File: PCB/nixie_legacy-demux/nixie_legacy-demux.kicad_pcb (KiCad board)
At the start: 2 copper layers, 106.7 x 112 mm, 37 parts, among them J3 HEADER_18, J5 HEADER_4, K155ID1 K155ID1

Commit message: Adding demux PCB v1: uses resistor network for 100k, has npn on board but pnp is on digit board
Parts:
- removed the 22pF at (123.2, 103.9)
- removed the 22pF at (124.5, 122.4)
- removed R 100k: 100k, Resistor_THT:R_Axial_DIN0207_L6.3mm_D2.5mm_P7.62mm_Horizontal (x5)
- removed the R 470k at (70.6, 15.0)
- added 100k Network: 100k, Resistor_THT:R_Array_SIP7, F.Cu at (126.0, 68.1)
- added 22pF: 22pF, Capacitor_THT:C_Disc_D3.0mm_W1.6mm_P2.50mm, F.Cu at (125.0, 106.2)
- added 22pF: 22pF, Capacitor_THT:C_Disc_D3.0mm_W1.6mm_P2.50mm, F.Cu at (125.0, 121.4)
- R 3k3: renamed from R 3.3k (x2)
- R 470k: renamed from R6
- moved R 470k 59.2 mm to (119.4, 77.5)
- moved R 470k 55.7 mm to (114.8, 71.4), turned to 180 degrees
- moved R 470k 55.3 mm to (114.8, 77.5), turned to 180 degrees
- moved R 470k 55.2 mm to (114.8, 74.4), turned to 180 degrees
- moved MPSA42 53.5 mm to (121.9, 86.6)
- moved R 33k 50.0 mm to (114.8, 90.7), turned to 180 degrees
- moved MPSA42 49.0 mm to (114.6, 86.6)
- moved R 470k 48.7 mm to (119.4, 74.4)
- moved R 33k 48.5 mm to (114.8, 96.8), turned to 180 degrees
- moved R 33k 47.9 mm to (114.8, 93.7), turned to 180 degrees
- moved MPSA42 47.6 mm to (107.2, 86.6)
- moved MPSA42 38.7 mm to (127.0, 81.0), turned to 180 degrees
- moved R 470k 38.6 mm to (119.4, 71.4)
- moved GND,Sel,Up,Dn 30.4 mm to (119.4, 151.4), turned to 90 degrees
- moved J3 27.5 mm to (134.6, 88.1), turned to 180 degrees
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- renumbered ATMEGA328P to ATmega328p, J5 to GND,Sel,Up,Dn
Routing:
- net 5v: track 0.00 -> 161.5 mm
- net 200v: track 0.00 -> 104.7 mm
- net 5: track 0.00 -> 44.8 mm
- net 1: track 0.00 -> 40.7 mm
- net 9: track 0.00 -> 38.6 mm
- net digit6lsb: track 0.00 -> 37.8 mm
- net Net-(J5-Pad4): track 0.00 -> 37.6 mm
- net Net-(R18-Pad2): track 0.00 -> 35.5 mm
- net 8: track 0.00 -> 34.7 mm
- net Net-(J2-Pad7): track 0.00 -> 34.4 mm
- net 0: track 0.00 -> 34.3 mm
- net 4: track 0.00 -> 34.3 mm
- net Net-(U1-Pad13): track 0.00 -> 34.1 mm
- net Net-(J5-Pad3): track 0.00 -> 33.2 mm
- net Net-(U1-Pad14): track 0.00 -> 33.1 mm
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- added copper zone on B.Cu, net GND
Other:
- board size 106.7 x 112 mm -> 35.6 x 99.1 mm
- board text added: "Nixie Demux v1"
- board text added: "WARNING: High Voltage"

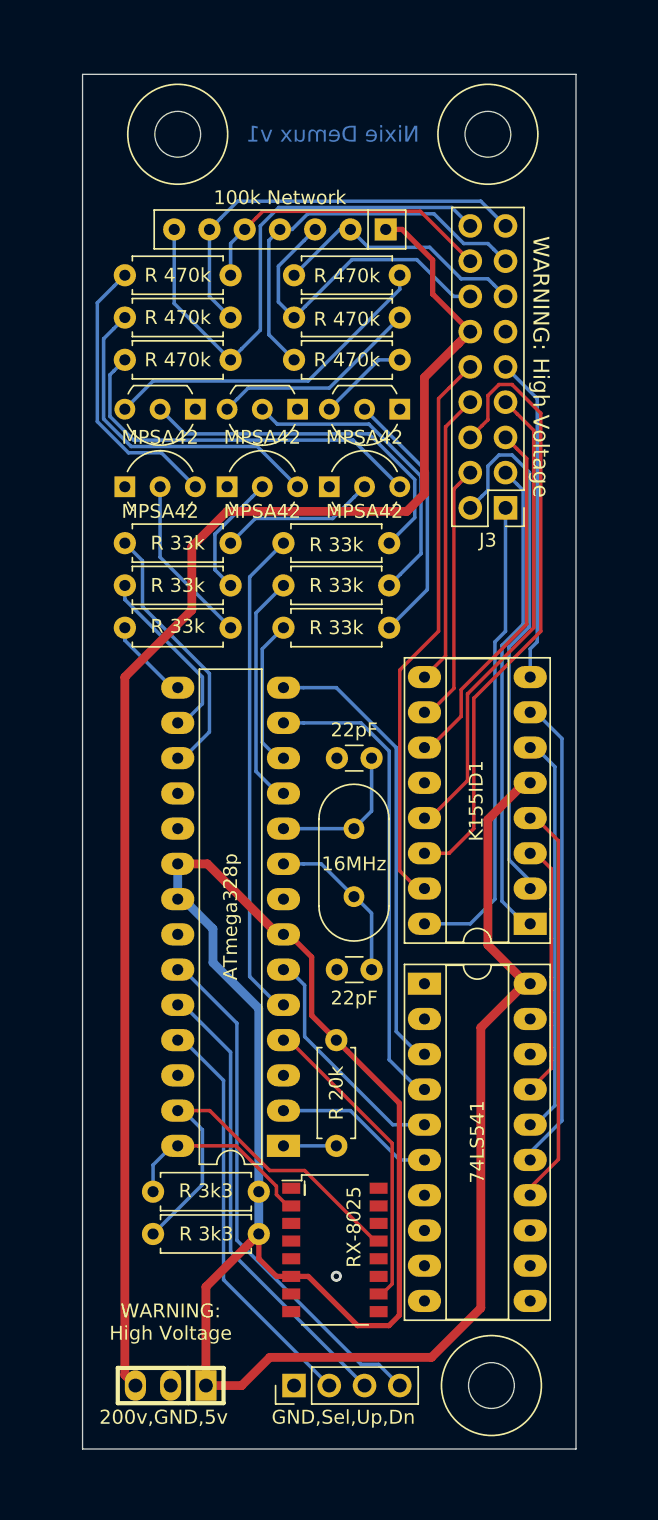
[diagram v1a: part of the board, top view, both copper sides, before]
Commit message: demux pcb v2, has MPSA92 transistors on this board instead of digit board, reducing connector to 16 pins instead of 18.
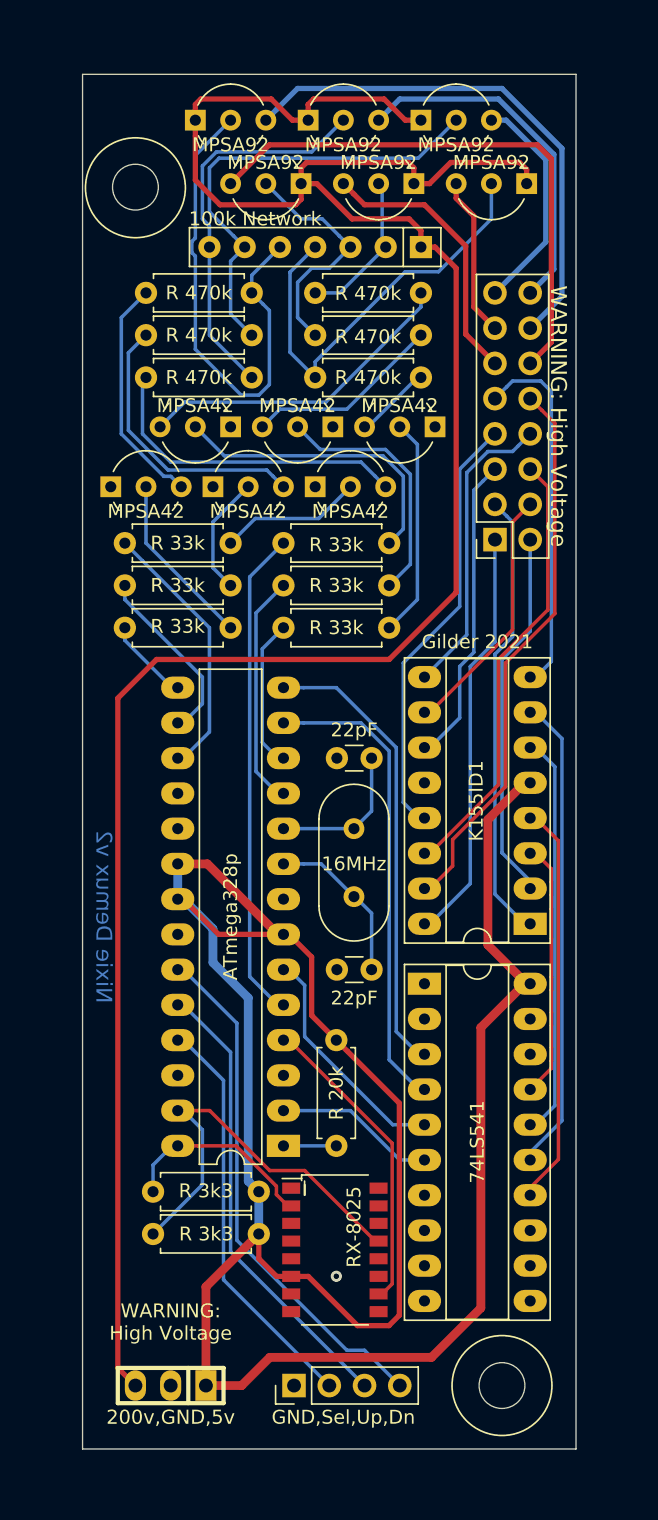
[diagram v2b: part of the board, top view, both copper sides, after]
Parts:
- removed J3: HEADER_18, Connector_PinHeader_2.54mm:PinHeader_2x09_P2.54mm_Vertical
- removed the MPSA42 at (121.9, 86.6)
- removed the MPSA42 at (114.6, 86.6)
- removed the MPSA42 at (107.2, 86.6)
- removed the MPSA42 at (112.3, 81.0)
- removed the MPSA42 at (119.6, 81.0)
- removed the MPSA42 at (127.0, 81.0)
- added  : HEADER_16, Connector_PinSocket_2.54mm:PinSocket_2x08_P2.54mm_Vertical, F.Cu at (133.9, 90.4)
- added MPSA42: MPSA42, Package_TO_SOT_THT:TO-92L_Inline_Wide, F.Cu at (114.8, 82.3)
- added MPSA42: MPSA42, Package_TO_SOT_THT:TO-92L_Inline_Wide, F.Cu at (122.2, 82.3)
- added MPSA42: MPSA42, Package_TO_SOT_THT:TO-92L_Inline_Wide, F.Cu at (129.5, 82.3)
- added MPSA42: MPSA42, Package_TO_SOT_THT:TO-92L_Inline_Wide, F.Cu at (120.9, 86.6)
- added MPSA42: MPSA42, Package_TO_SOT_THT:TO-92L_Inline_Wide, F.Cu at (113.5, 86.6)
- added MPSA42: MPSA42, Package_TO_SOT_THT:TO-92L_Inline_Wide, F.Cu at (106.2, 86.6)
- added MPSA92: MPSA92, Package_TO_SOT_THT:TO-92L_Inline_Wide, F.Cu at (128.5, 60.2)
- added MPSA92: MPSA92, Package_TO_SOT_THT:TO-92L_Inline_Wide, F.Cu at (120.4, 60.2)
- added MPSA92: MPSA92, Package_TO_SOT_THT:TO-92L_Inline_Wide, F.Cu at (112.3, 60.2)
- added MPSA92: MPSA92, Package_TO_SOT_THT:TO-92L_Inline_Wide, F.Cu at (136.1, 64.8)
- added MPSA92: MPSA92, Package_TO_SOT_THT:TO-92L_Inline_Wide, F.Cu at (128.0, 64.8)
- added MPSA92: MPSA92, Package_TO_SOT_THT:TO-92L_Inline_Wide, F.Cu at (119.9, 64.8)
- moved 100k Network 2.84 mm to (128.5, 69.3)
- moved R 470k 1.98 mm to (120.9, 72.6)
- moved R 470k 1.98 mm to (120.9, 75.7)
- moved R 470k 1.98 mm to (120.9, 78.7)
- moved R 470k 1.98 mm to (116.3, 72.6)
- moved R 470k 1.98 mm to (116.3, 75.7)
- moved R 470k 1.98 mm to (116.3, 78.7)
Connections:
- net digit1msb renamed Net-(Q7-Pad2)
- net digit2 renamed Net-(Q8-Pad2)
- net digit3 renamed Net-(Q9-Pad2)
- net digit4 renamed Net-(Q10-Pad2)
- net digit5 renamed Net-(Q11-Pad2)
- net digit6lsb renamed Net-(Q12-Pad2)
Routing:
- net 200v: track 104.7 -> 170.1 mm
- net digit2: track 0.00 -> 40.1 mm
- net digit4: track 0.00 -> 38.0 mm
- net digit6lsb: track 0.00 -> 25.6 mm
- net digit1msb: track 0.00 -> 20.0 mm
- net digit5: track 0.00 -> 16.2 mm
- net Net-(Q10-Pad2): track 22.0 -> 36.1 mm
- net 5: track 44.8 -> 32.1 mm
- net 9: track 38.6 -> 26.8 mm
- net digit3: track 0.00 -> 11.6 mm
- net Net-(Q12-Pad2): track 37.8 -> 28.2 mm
- net 5v: track 161.5 -> 170.2 mm
- net Net-(Q7-Pad2): track 18.6 -> 11.2 mm
- net Net-(Q8-Pad2): track 23.4 -> 17.2 mm
- net 0: track 34.3 -> 30.0 mm
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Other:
- outline, holes or cut-outs redrawn
- board text added: "Gilder 2021"
- board text added: "Nixie Demux v2"
- board text removed: "Nixie Demux v1"

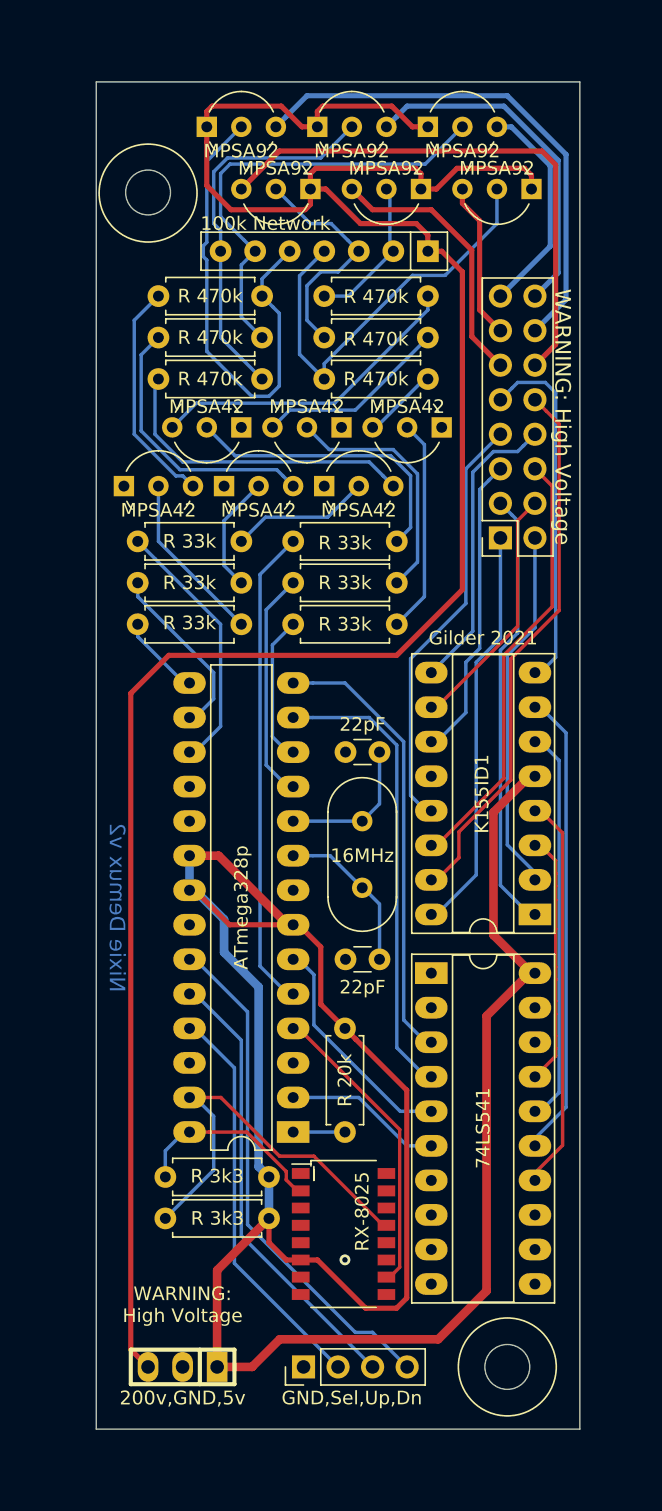
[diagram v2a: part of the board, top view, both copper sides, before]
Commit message: demux pcb update: footprint for rtc was sop 16 instead of sop 14. rerouted power traces. shortened to 3.75"
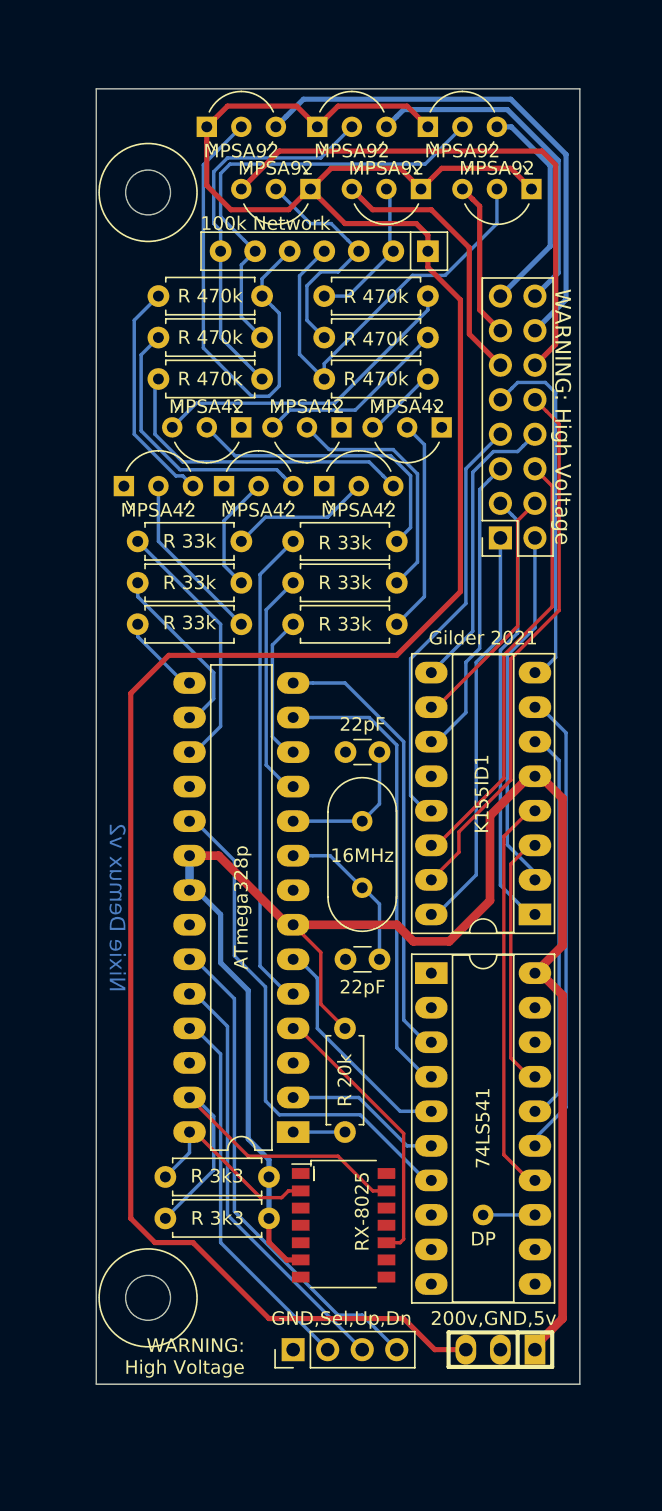
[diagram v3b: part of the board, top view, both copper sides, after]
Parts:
- added DP: Decimal Point, customPartsLibrary:Single_pad-1x1, F.Cu at (132.6, 140.2)
- moved 200v,GND,5v 23.4 mm to (133.9, 150.1)
- moved GND,Sel,Up,Dn 1.48 mm to (118.6, 150.1)
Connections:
- 74LS541 pad 7: Net-(U3-Pad7) -> Net-(U1-Pad19)
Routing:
- net 5v: track 170.2 -> 127.4 mm
- net Net-(U1-Pad19): track 0.00 -> 37.7 mm
- net 200v: track 170.1 -> 182.7 mm
- net Net-(JP1-Pad1): track 0.00 -> 3.81 mm
- net Net-(J4-Pad10): track 22.3 -> 20.5 mm
- net Net-(J5-Pad3): track 33.2 -> 31.7 mm
- net Net-(J5-Pad2): track 29.7 -> 28.1 mm
- net Net-(J5-Pad4): track 37.6 -> 36.3 mm
- net Net-(J4-Pad13): track 29.7 -> 28.7 mm
- net GND: vias 1 -> 0
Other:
- board size 35.6 x 99.1 mm -> 35.6 x 95.2 mm
